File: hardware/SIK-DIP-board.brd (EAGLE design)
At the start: 91.4 x 66 mm, 76 parts

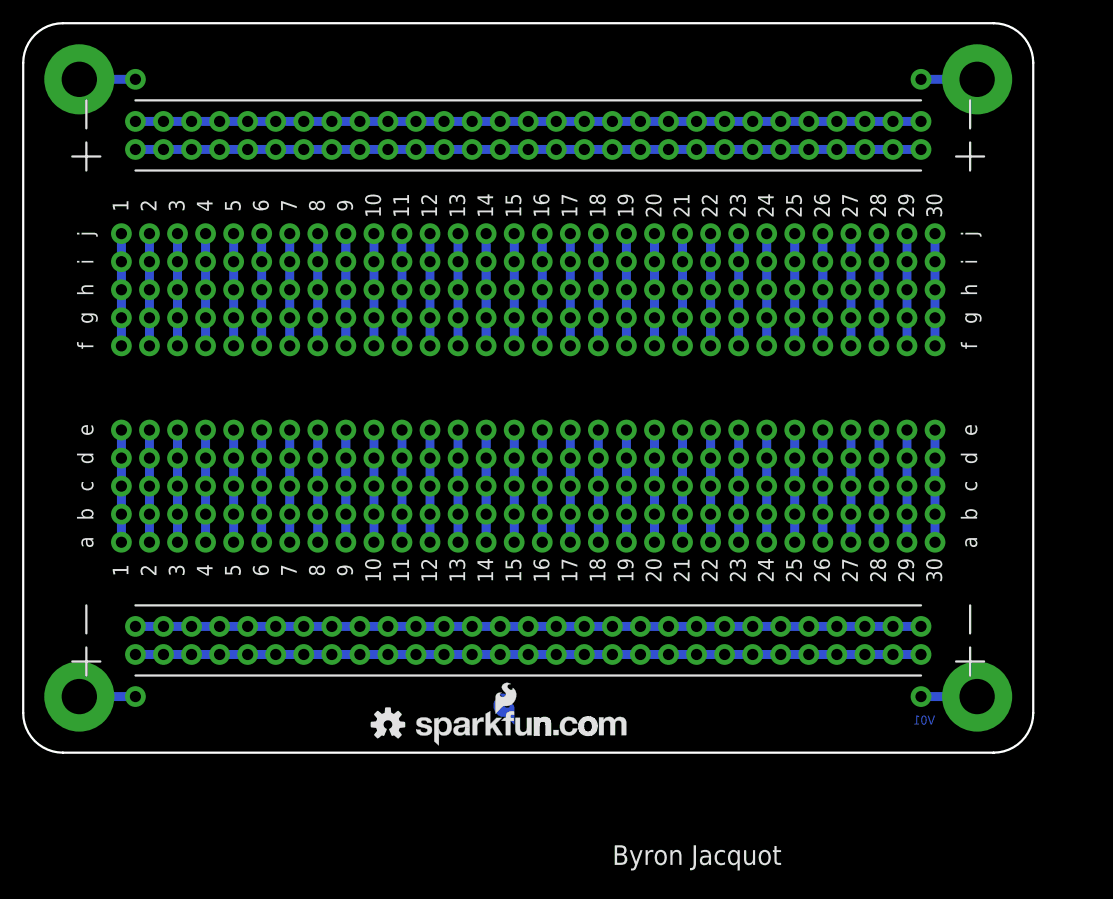
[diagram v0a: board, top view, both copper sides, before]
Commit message: Amended following group review
Adjusted size so silk doesn't overlap mounting holes.
Duplicated top silk on bottom.
Added name.
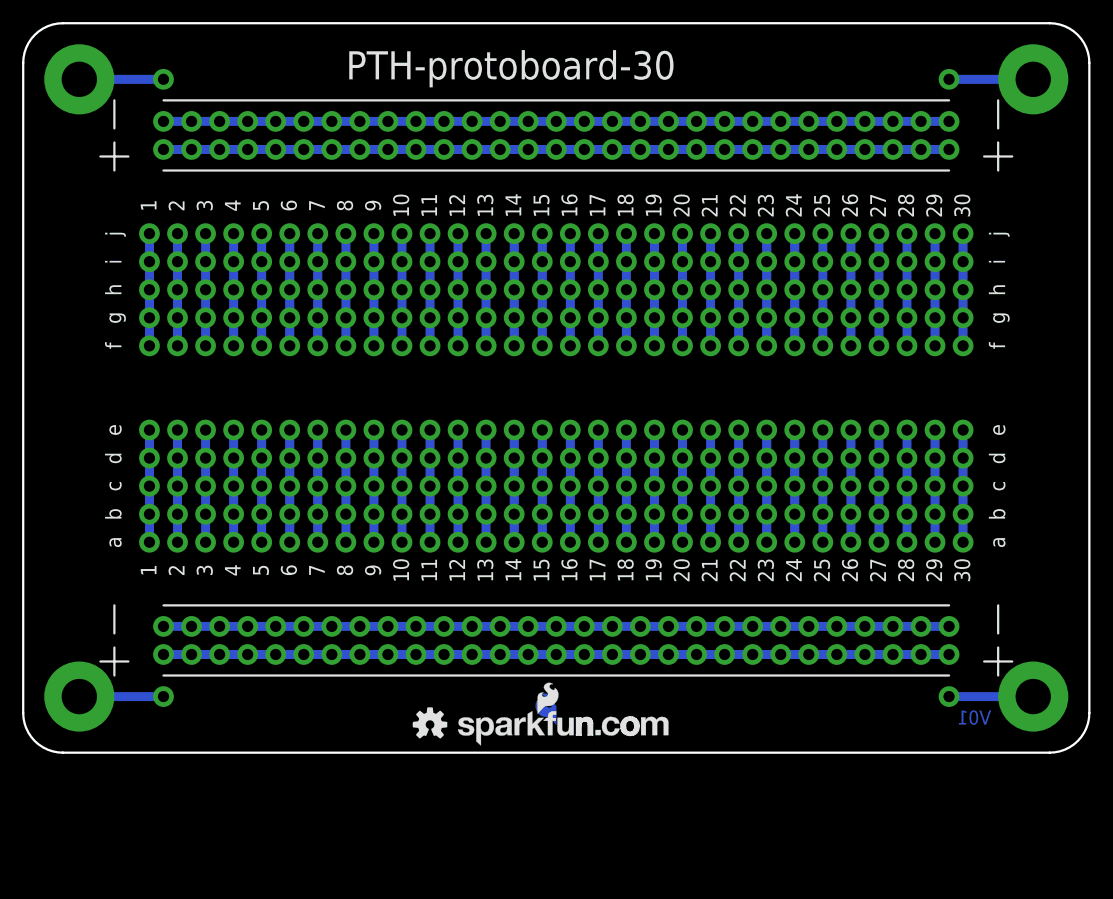
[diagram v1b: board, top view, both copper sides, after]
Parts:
- moved S2 5.08 mm to (91.4, 61.0)
- moved S4 5.08 mm to (91.4, 5.08)
- moved LOGO1 3.81 mm to (48.3, 2.54)
- moved LOGO2 3.81 mm to (39.4, 0.64)
- moved LOGO3 3.81 mm to (36.8, 2.54)
- moved JP18 2.54 mm to (44.5, 19.1)
- moved JP27 2.54 mm to (67.3, 19.1)
- moved JP29 2.54 mm to (72.4, 19.1)
- moved JP30 2.54 mm to (74.9, 19.1)
- moved JP32 2.54 mm to (80.0, 19.1)
- moved JP34 2.54 mm to (85.1, 19.1)
- moved JP48 2.54 mm to (44.5, 36.8)
- moved JP57 2.54 mm to (67.3, 36.8)
- moved JP59 2.54 mm to (72.4, 36.8)
- moved JP60 2.54 mm to (74.9, 36.8)
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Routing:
- net N$68: track 5.08 -> 7.62 mm
- net N$65: track 5.08 -> 7.62 mm
- net N$67: track 5.08 -> 7.62 mm
- net N$66: track 5.08 -> 7.62 mm
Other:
- board size 91.4 x 66 mm -> 96.5 x 66 mm
- board text added: "PTH-protoboard-30"
